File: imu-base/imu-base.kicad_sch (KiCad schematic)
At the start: 17 parts, among them J1 1374028, J2 DE9_Plug_MountingHoles, U1 AP2204K-ADJ

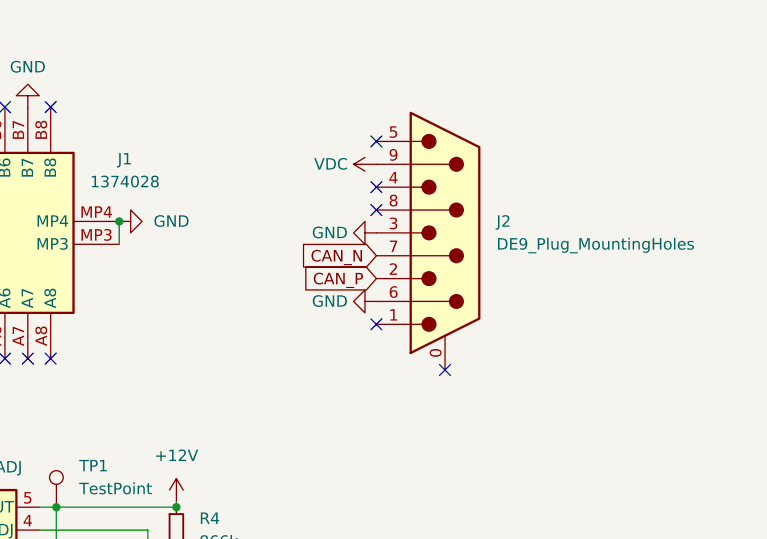
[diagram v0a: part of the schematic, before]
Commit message: fix: CAN pin error
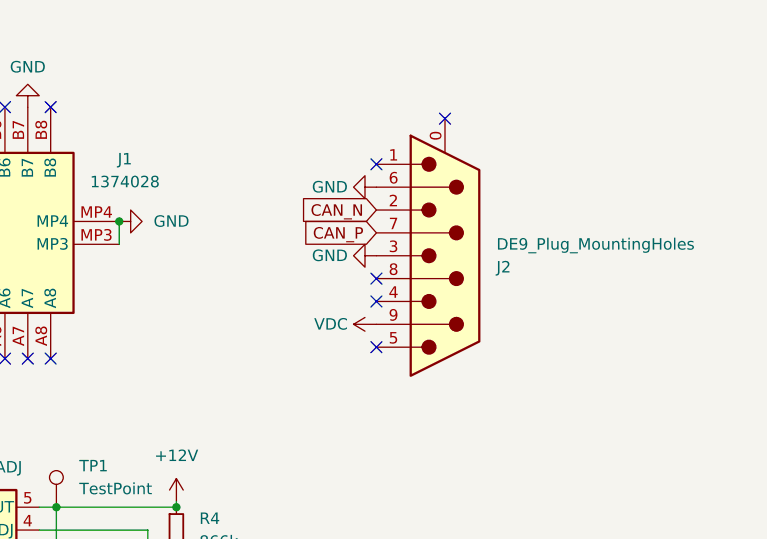
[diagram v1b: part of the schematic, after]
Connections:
- net CAN_N: now also J2.2; no longer J2.7
- net CAN_P: now also J2.7; no longer J2.2
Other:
- moved on the sheet: J2
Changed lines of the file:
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@@
   )
   (no_connect (at 35.56 30.48))
-  (no_connect (at 116.84 36.83))
+  (no_connect (at 116.84 44.45))
   (no_connect (at 75.565 25.4))
-  (no_connect (at 116.84 34.29))
+  (no_connect (at 116.84 46.99))
   (no_connect (at 73.025 53.34))
   (no_connect (at 78.105 53.34))
   (no_connect (at 75.565 53.34))
-  (no_connect (at 116.84 49.53))
+  (no_connect (at 116.84 31.75))
   (no_connect (at 80.645 25.4))
-  (no_connect (at 124.46 54.61))
+  (no_connect (at 124.46 26.67))
   (no_connect (at 67.945 53.34))
   (no_connect (at 67.945 25.4))
@@
   (no_connect (at 73.025 25.4))
   (no_connect (at 80.645 53.34))
-  (no_connect (at 116.84 29.21))
+  (no_connect (at 116.84 52.07))
   (wire (pts (xy 58.42 69.85) (xy 58.42 72.39))
     (stroke (width 0) (type default))
@@
     (stroke (width 0) (type default))
   )
-  (global_label "CAN_N" (shape input) (at 116.84 41.91 180) (fields_autoplaced)
+  (global_label "CAN_N" (shape input) (at 116.84 36.83 180) (fields_autoplaced)
     (effects (font (size 1.27 1.27)) (justify right))
-    (property "Intersheetrefs" "${INTERSHEET_REFS}" (at 107.8676 41.91 0)
+    (property "Intersheetrefs" "${INTERSHEET_REFS}" (at 107.8676 36.83 0)
       (effects (font (size 1.27 1.27)) (justify right) hide)
     )
@@
     )
   )
-  (global_label "CAN_P" (shape input) (at 116.84 44.45 180) (fields_autoplaced)
+  (global_label "CAN_P" (shape input) (at 116.84 39.37 180) (fields_autoplaced)
     (effects (font (size 1.27 1.27)) (justify right))
-    (property "Intersheetrefs" "${INTERSHEET_REFS}" (at 107.9281 44.45 0)
+    (property "Intersheetrefs" "${INTERSHEET_REFS}" (at 107.9281 39.37 0)
       (effects (font (size 1.27 1.27)) (justify right) hide)
     )
@@
     )
   )
-  (symbol (lib_id "Connector:DE9_Plug_MountingHoles") (at 124.46 39.37 0) (unit 1)
-    (in_bom yes) (on_board yes) (dnp no) (fields_autoplaced)
-    (property "Reference" "J2" (at 130.175 38.1 0)
+  (symbol (lib_id "Connector:DE9_Plug_MountingHoles") (at 124.46 41.91 0) (mirror x) (unit 1)
+    (in_bom yes) (on_board yes) (dnp no) (fields_autoplaced)
+    (property "Reference" "J2" (at 130.175 43.18 0)
       (effects (font (size 1.27 1.27)) (justify left))
     )
@@
       (effects (font (size 1.27 1.27)) (justify left))
     )
-    (property "Footprint" "Connector_Dsub:DSUB-9_Female_Horizontal_P2.77x2.84mm_EdgePinOffset7.70mm_Housed_MountingHolesOffset9.12mm" (at 124.46 39.37 0)
-      (effects (font (size 1.27 1.27)) hide)
-    )
-    (property "Datasheet" " ~" (at 124.46 39.37 0)
+    (property "Footprint" "Connector_Dsub:DSUB-9_Female_Horizontal_P2.77x2.84mm_EdgePinOffset7.70mm_Housed_MountingHolesOffset9.12mm" (at 124.46 41.91 0)
+      (effects (font (size 1.27 1.27)) hide)
+    )
+    (property "Datasheet" " ~" (at 124.46 41.91 0)
       (effects (font (size 1.27 1.27)) hide)
     )
@@
     )
   )
-  (symbol (lib_id "power:GND") (at 116.84 46.99 270) (unit 1)
-    (in_bom yes) (on_board yes) (dnp no) (fields_autoplaced)
-    (property "Reference" "#PWR019" (at 110.49 46.99 0)
-      (effects (font (size 1.27 1.27)) hide)
-    )
-    (property "Value" "GND" (at 113.665 46.99 90)
-      (effects (font (size 1.27 1.27)) (justify right))
-    )
-    (property "Footprint" "" (at 116.84 46.99 0)
-      (effects (font (size 1.27 1.27)) hide)
-    )
-    (property "Datasheet" "" (at 116.84 46.99 0)
+  (symbol (lib_id "power:GND") (at 116.84 34.29 270) (mirror x) (unit 1)
+    (in_bom yes) (on_board yes) (dnp no) (fields_autoplaced)
+    (property "Reference" "#PWR019" (at 110.49 34.29 0)
+      (effects (font (size 1.27 1.27)) hide)
+    )
+    (property "Value" "GND" (at 113.665 34.29 90)
+      (effects (font (size 1.27 1.27)) (justify right))
+    )
+    (property "Footprint" "" (at 116.84 34.29 0)
+      (effects (font (size 1.27 1.27)) hide)
+    )
+    (property "Datasheet" "" (at 116.84 34.29 0)
       (effects (font (size 1.27 1.27)) hide)
     )
@@
     )
   )
-  (symbol (lib_id "power:VDC") (at 116.84 31.75 90) (unit 1)
-    (in_bom yes) (on_board yes) (dnp no) (fields_autoplaced)
-    (property "Reference" "#PWR017" (at 119.38 31.75 0)
-      (effects (font (size 1.27 1.27)) hide)
-    )
-    (property "Value" "VDC" (at 113.665 31.75 90)
+  (symbol (lib_id "power:VDC") (at 116.84 49.53 90) (mirror x) (unit 1)
+    (in_bom yes) (on_board yes) (dnp no) (fields_autoplaced)
+    (property "Reference" "#PWR017" (at 119.38 49.53 0)
+      (effects (font (size 1.27 1.27)) hide)
+    )
+    (property "Value" "VDC" (at 113.665 49.53 90)
       (effects (font (size 1.27 1.27)) (justify left))
     )
-    (property "Footprint" "" (at 116.84 31.75 0)
-      (effects (font (size 1.27 1.27)) hide)
-    )
-    (property "Datasheet" "" (at 116.84 31.75 0)
+    (property "Footprint" "" (at 116.84 49.53 0)
+      (effects (font (size 1.27 1.27)) hide)
+    )
+    (property "Datasheet" "" (at 116.84 49.53 0)
       (effects (font (size 1.27 1.27)) hide)
     )
@@
     )
   )
-  (symbol (lib_id "power:GND") (at 116.84 39.37 270) (unit 1)
-    (in_bom yes) (on_board yes) (dnp no) (fields_autoplaced)
-    (property "Reference" "#PWR018" (at 110.49 39.37 0)
-      (effects (font (size 1.27 1.27)) hide)
-    )
-    (property "Value" "GND" (at 113.665 39.37 90)
-      (effects (font (size 1.27 1.27)) (justify right))
-    )
-    (property "Footprint" "" (at 116.84 39.37 0)
-      (effects (font (size 1.27 1.27)) hide)
-    )
-    (property "Datasheet" "" (at 116.84 39.37 0)
-      (effects (font (size 1.27 1.27)) hide)
-    )
+  (symbol (lib_id "power:GND") (at 116.84 41.91 270) (mirror x) (unit 1)
+    (in_bom yes) (on_board yes) (dnp no) (fields_autoplaced)
+    (property "Reference" "#PWR018" (at 110.49 41.91 0)
+      (effects (font (size 1.27 1.27)) hide)
+    )
+    (property "Value" "GND" (at 113.665 41.91 90)
+      (effects (font (size 1.27 1.27)) (justify right))
+    )
+    (property "Footprint" "" (at 116.84 41.91 0)
+      (effects (font (size 1.27 1.27)) hide)
+    )
+    (property "Datasheet" "" (at 116.84 41.91 0)
+      (effects (font (size 1.27 1.27)) hide)
+    )
